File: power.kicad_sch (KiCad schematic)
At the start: 4 parts

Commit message: working on powers
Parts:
- added C17: C-Pol-10uF-TAN, Capacitor_Tantalum_SMD:CP_EIA-6032-28_Kemet-C, symbol eurorack:C-Pol-10uF-TAN
- added RV11: Trim_5k_prec_tht, eurorack:trim_2.5mm, symbol eurorack:Trim_5k_prec_tht
- added U10: TL072, Package_SO:SO-8_3.9x4.9mm_P1.27mm, symbol eurorack:TL072
- added U9: ZLDO1117G33TA, Package_TO_SOT_SMD:SOT-223, symbol eurorack:ZLDO1117G33TA
- gave numbers to parts that had none: 4
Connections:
- net +12V: now also U10.8 (V+)
- net +5V: now also U9.3 (IN)
- net -12V: now also RV11.3, U10.4 (V-)
- net GND: now also C17.2, RV11.1, U10.5 (+), U9.1 (ADJ)
- new net: RV11.2, U10.3 (+)
- new net: U10.6 (-), U10.7
- new net +3V3: C17.1, U9.2 (OUT), U9.4 (OUT)
- new net -1V65: U10.1, U10.2 (-)

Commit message: WIP
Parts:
- added C?: C-Pol-1uF-FK-V, Capacitor_SMD:C_1206_3216Metric, symbol eurorack:C-Pol-1uF-FK-V
- added C?: C-Pol-10uF-FK-V, Capacitor_SMD:CP_Elec_8x6.2, symbol eurorack:C-Pol-10uF-FK-V
- added C? (x2): C-100nF-0805, Capacitor_SMD:C_0805_2012Metric_Pad1.18x1.45mm_HandSolder, symbol eurorack:C-100nF-0805
- added U?: REF191, Package_SO:SO-8_3.9x4.9mm_P1.27mm, symbol eurorack:REF191
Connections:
- net +3V3: now also C?.1, C?.1, U?.2 (Vin), U?.3 (~{Sleep})
- net GND: now also C?.2, C?.2, C?.2, C?.2, U?.4 (GND)
- new net 1V25: C?.1, C?.1, U?.6 (Vout)

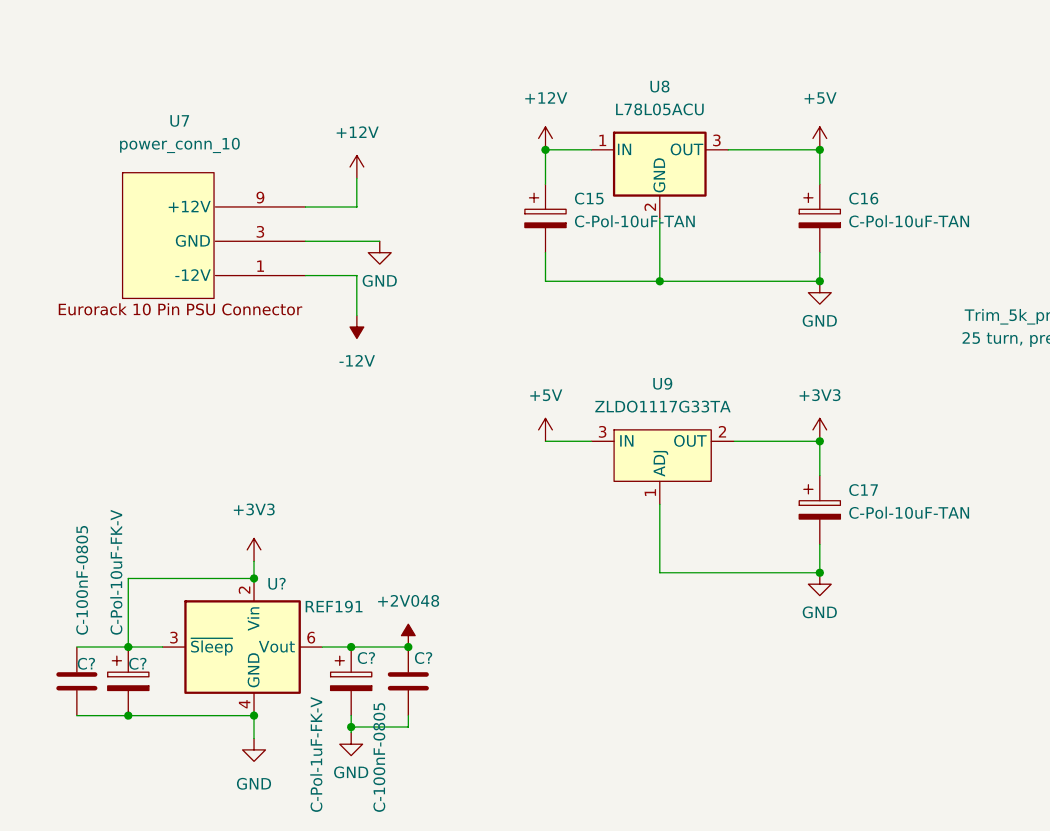
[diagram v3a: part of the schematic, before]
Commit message: refactoring with global labels
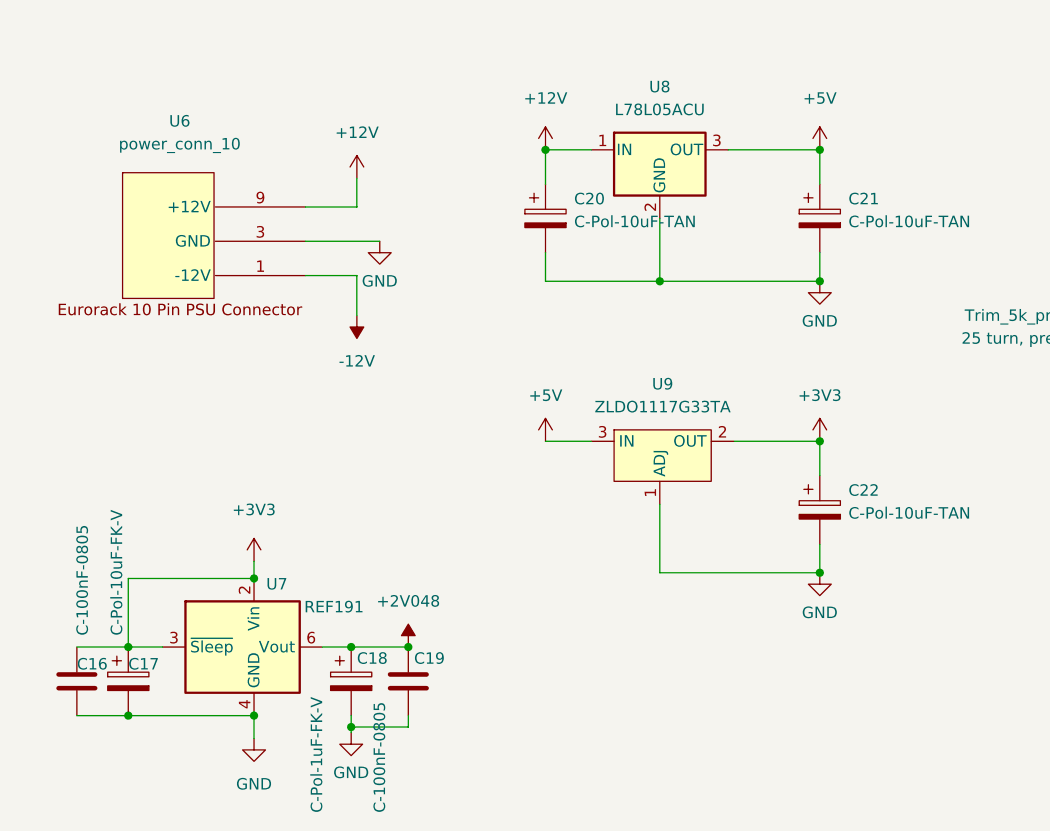
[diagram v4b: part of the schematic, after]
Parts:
- gave numbers to parts that had none: 5
- renumbered C15 to C20, C16 to C21, C17 to C22, U7 to U6
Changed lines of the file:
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@@
   (symbol (lib_id "eurorack:power_conn_10") (at 37.465 32.385 0) (unit 1)
     (in_bom yes) (on_board yes) (fields_autoplaced)
-    (property "Reference" "U7" (id 0) (at 38.735 25.4 0))
+    (property "Reference" "U6" (id 0) (at 38.735 25.4 0))
     (property "Value" "power_conn_10" (id 1) (at 38.735 27.94 0))
     (property "Footprint" "eurorack:power_10" (id 2) (at 40.005 48.895 0)
@@
   (symbol (lib_id "power:-12V") (at 143.51 52.705 180) (unit 1)
     (in_bom yes) (on_board yes) (fields_autoplaced)
-    (property "Reference" "#PWR070" (id 0) (at 143.51 55.245 0)
+    (property "Reference" "#PWR080" (id 0) (at 143.51 55.245 0)
       (effects (font (size 1.27 1.27)) hide)
     )
@@
   (symbol (lib_id "power:+12V") (at 79.375 28.575 0) (unit 1)
     (in_bom yes) (on_board yes) (fields_autoplaced)
-    (property "Reference" "#PWR064" (id 0) (at 79.375 32.385 0)
+    (property "Reference" "#PWR074" (id 0) (at 79.375 32.385 0)
       (effects (font (size 1.27 1.27)) hide)
     )
@@
   (symbol (lib_id "power:GND") (at 109.855 75.565 0) (unit 1)
     (in_bom yes) (on_board yes) (fields_autoplaced)
-    (property "Reference" "#PWR069" (id 0) (at 109.855 81.915 0)
+    (property "Reference" "#PWR079" (id 0) (at 109.855 81.915 0)
       (effects (font (size 1.27 1.27)) hide)
     )
@@
   (symbol (lib_id "power:+5V") (at 79.375 60.96 0) (unit 1)
     (in_bom yes) (on_board yes) (fields_autoplaced)
-    (property "Reference" "#PWR065" (id 0) (at 79.375 64.77 0)
+    (property "Reference" "#PWR075" (id 0) (at 79.375 64.77 0)
       (effects (font (size 1.27 1.27)) hide)
     )
@@
   (symbol (lib_id "eurorack:C-Pol-1uF-FK-V") (at 57.785 87.63 0) (unit 1)
     (in_bom yes) (on_board yes)
-    (property "Reference" "C?" (id 0) (at 58.42 85.09 0)
+    (property "Reference" "C18" (id 0) (at 58.42 85.09 0)
       (effects (font (size 1.27 1.27)) (justify left))
     )
@@
   (symbol (lib_id "power:GND") (at 46.99 93.98 0) (unit 1)
     (in_bom yes) (on_board yes) (fields_autoplaced)
-    (property "Reference" "#PWR?" (id 0) (at 46.99 100.33 0)
+    (property "Reference" "#PWR068" (id 0) (at 46.99 100.33 0)
       (effects (font (size 1.27 1.27)) hide)
     )
@@
   (symbol (lib_id "power:-12V") (at 274.32 38.735 180) (unit 1)
     (in_bom yes) (on_board yes) (fields_autoplaced)
-    (property "Reference" "#PWR075" (id 0) (at 274.32 41.275 0)
+    (property "Reference" "#PWR085" (id 0) (at 274.32 41.275 0)
       (effects (font (size 1.27 1.27)) hide)
     )
@@
   (symbol (lib_id "eurorack:C-Pol-10uF-TAN") (at 109.855 36.195 0) (unit 1)
     (in_bom yes) (on_board yes) (fields_autoplaced)
-    (property "Reference" "C16" (id 0) (at 113.03 34.0359 0)
+    (property "Reference" "C21" (id 0) (at 113.03 34.0359 0)
       (effects (font (size 1.27 1.27)) (justify left))
     )
@@
   (symbol (lib_id "eurorack:C-Pol-10uF-FK-V") (at 33.02 87.63 0) (unit 1)
     (in_bom yes) (on_board yes)
-    (property "Reference" "C?" (id 0) (at 33.02 85.725 0)
+    (property "Reference" "C17" (id 0) (at 33.02 85.725 0)
       (effects (font (size 1.27 1.27)) (justify left))
     )
@@
   (symbol (lib_id "eurorack:C-100nF-0805") (at 64.135 87.63 0) (unit 1)
     (in_bom yes) (on_board yes)
-    (property "Reference" "C?" (id 0) (at 64.77 85.09 0)
+    (property "Reference" "C19" (id 0) (at 64.77 85.09 0)
       (effects (font (size 1.27 1.27)) (justify left))
     )
@@
   (symbol (lib_id "power:GND") (at 57.785 93.345 0) (unit 1)
     (in_bom yes) (on_board yes) (fields_autoplaced)
-    (property "Reference" "#PWR?" (id 0) (at 57.785 99.695 0)
+    (property "Reference" "#PWR069" (id 0) (at 57.785 99.695 0)
       (effects (font (size 1.27 1.27)) hide)
     )
@@
   (symbol (lib_id "eurorack:C-100nF-0805") (at 27.305 87.63 0) (unit 1)
     (in_bom yes) (on_board yes)
-    (property "Reference" "C?" (id 0) (at 27.305 85.725 0)
+    (property "Reference" "C16" (id 0) (at 27.305 85.725 0)
       (effects (font (size 1.27 1.27)) (justify left))
     )
@@
   (symbol (lib_id "power:+5V") (at 109.855 28.575 0) (unit 1)
     (in_bom yes) (on_board yes) (fields_autoplaced)
-    (property "Reference" "#PWR066" (id 0) (at 109.855 32.385 0)
+    (property "Reference" "#PWR076" (id 0) (at 109.855 32.385 0)
       (effects (font (size 1.27 1.27)) hide)
     )
@@
   (symbol (lib_id "power:+3V3") (at 109.855 60.96 0) (unit 1)
     (in_bom yes) (on_board yes) (fields_autoplaced)
-    (property "Reference" "#PWR068" (id 0) (at 109.855 64.77 0)
+    (property "Reference" "#PWR078" (id 0) (at 109.855 64.77 0)
       (effects (font (size 1.27 1.27)) hide)
     )
@@
   (symbol (lib_id "power:GND") (at 60.96 38.735 0) (unit 1)
     (in_bom yes) (on_board yes) (fields_autoplaced)
-    (property "Reference" "#PWR063" (id 0) (at 60.96 45.085 0)
+    (property "Reference" "#PWR072" (id 0) (at 60.96 45.085 0)
       (effects (font (size 1.27 1.27)) hide)
     )
@@
   (symbol (lib_id "eurorack:C-Pol-10uF-TAN") (at 79.375 36.195 0) (unit 1)
     (in_bom yes) (on_board yes) (fields_autoplaced)
-    (property "Reference" "C15" (id 0) (at 82.55 34.0359 0)
+    (property "Reference" "C20" (id 0) (at 82.55 34.0359 0)
       (effects (font (size 1.27 1.27)) (justify left))
     )
@@
   (symbol (lib_id "power:+3V3") (at 46.99 74.295 0) (unit 1)
     (in_bom yes) (on_board yes) (fields_autoplaced)
-    (property "Reference" "#PWR?" (id 0) (at 46.99 78.105 0)
+    (property "Reference" "#PWR067" (id 0) (at 46.99 78.105 0)
       (effects (font (size 1.27 1.27)) hide)
     )
@@
   (symbol (lib_id "eurorack:C-Pol-10uF-TAN") (at 109.855 68.58 0) (unit 1)
     (in_bom yes) (on_board yes) (fields_autoplaced)
-    (property "Reference" "C17" (id 0) (at 113.03 66.4209 0)
+    (property "Reference" "C22" (id 0) (at 113.03 66.4209 0)
       (effects (font (size 1.27 1.27)) (justify left))
     )
@@
   (symbol (lib_id "eurorack:REF191") (at 46.99 83.82 0) (unit 1)
     (in_bom yes) (on_board yes)
-    (property "Reference" "U?" (id 0) (at 49.53 76.835 0))
+    (property "Reference" "U7" (id 0) (at 49.53 76.835 0))
     (property "Value" "REF191" (id 1) (at 55.88 79.375 0))
     (property "Footprint" "Package_SO:SO-8_3.9x4.9mm_P1.27mm" (id 2) (at 46.99 85.09 0)
@@
   (symbol (lib_id "power:GND") (at 109.855 43.18 0) (unit 1)
     (in_bom yes) (on_board yes) (fields_autoplaced)
-    (property "Reference" "#PWR067" (id 0) (at 109.855 49.53 0)
+    (property "Reference" "#PWR077" (id 0) (at 109.855 49.53 0)
       (effects (font (size 1.27 1.27)) hide)
     )
@@
   (symbol (lib_id "power:+12V") (at 274.32 20.955 0) (unit 1)
     (in_bom yes) (on_board yes) (fields_autoplaced)
-    (property "Reference" "#PWR074" (id 0) (at 274.32 24.765 0)
+    (property "Reference" "#PWR084" (id 0) (at 274.32 24.765 0)
       (effects (font (size 1.27 1.27)) hide)
     )
@@
   (symbol (lib_id "power:GND") (at 148.59 39.37 0) (unit 1)
     (in_bom yes) (on_board yes) (fields_autoplaced)
-    (property "Reference" "#PWR071" (id 0) (at 148.59 45.72 0)
+    (property "Reference" "#PWR081" (id 0) (at 148.59 45.72 0)
       (effects (font (size 1.27 1.27)) hide)
     )
@@
   (symbol (lib_id "power:+12V") (at 58.42 31.75 0) (unit 1)
     (in_bom yes) (on_board yes) (fields_autoplaced)
-    (property "Reference" "#PWR061" (id 0) (at 58.42 35.56 0)
+    (property "Reference" "#PWR070" (id 0) (at 58.42 35.56 0)
       (effects (font (size 1.27 1.27)) hide)
     )
@@
   (symbol (lib_id "power:GND") (at 153.67 77.47 0) (mirror y) (unit 1)
     (in_bom yes) (on_board yes) (fields_autoplaced)
-    (property "Reference" "#PWR072" (id 0) (at 153.67 83.82 0)
+    (property "Reference" "#PWR082" (id 0) (at 153.67 83.82 0)
       (effects (font (size 1.27 1.27)) hide)
     )
@@
   (symbol (lib_id "power:-12V") (at 58.42 46.99 180) (unit 1)
     (in_bom yes) (on_board yes) (fields_autoplaced)
-    (property "Reference" "#PWR062" (id 0) (at 58.42 49.53 0)
+    (property "Reference" "#PWR071" (id 0) (at 58.42 49.53 0)
       (effects (font (size 1.27 1.27)) hide)
     )
@@
   (symbol (lib_id "eurorack:-1V65") (at 175.26 49.53 180) (unit 1)
     (in_bom yes) (on_board yes) (fields_autoplaced)
-    (property "Reference" "#PWR073" (id 0) (at 175.26 52.07 0)
+    (property "Reference" "#PWR083" (id 0) (at 175.26 52.07 0)
       (effects (font (size 1.27 1.27)) hide)
     )
@@
   (symbol (lib_id "eurorack:+2V048") (at 64.135 83.82 0) (unit 1)
     (in_bom yes) (on_board yes) (fields_autoplaced)
-    (property "Reference" "#PWR?" (id 0) (at 64.135 81.28 0)
-      (effects (font (size 1.27 1.27)) hide)
-    )
+    (property "Reference" "#PWR073" (id 0) (at 64.135 81.28 0)
+      (effects (font (size 1.27 1.27)) hide)
+    )

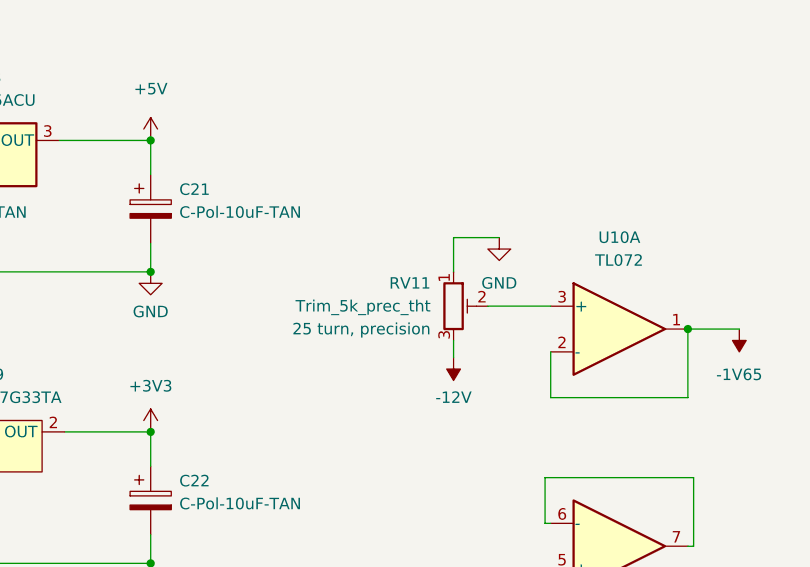
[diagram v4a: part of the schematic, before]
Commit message: cleaning into modules
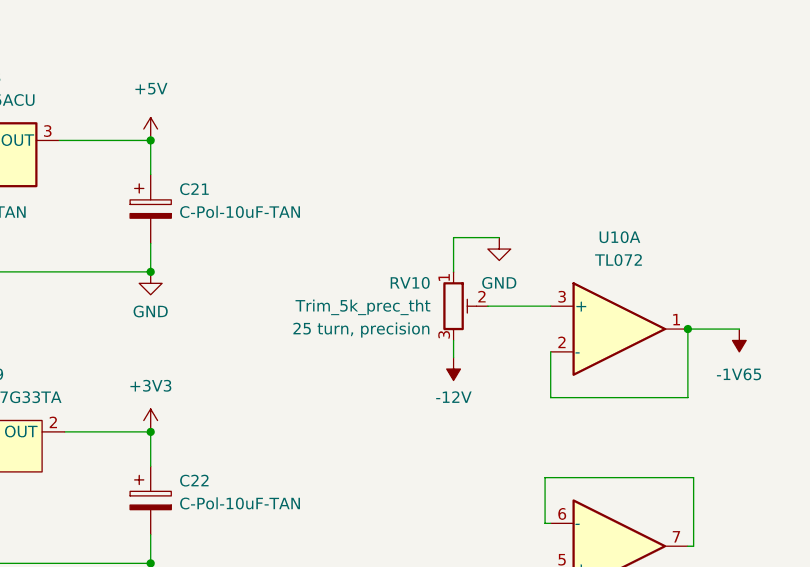
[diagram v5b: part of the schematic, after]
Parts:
- renumbered RV11 to RV10

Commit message: working on AD inputs
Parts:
- removed C18: C-Pol-1uF-FK-V, Capacitor_SMD:C_1206_3216Metric, symbol eurorack:C-Pol-1uF-FK-V
- added C18: C-Pol-1uF-TAN, Capacitor_Tantalum_SMD:CP_EIA-3216-18_Kemet-A, symbol eurorack:C-Pol-1uF-TAN
- renumbered U6 to U20, U7 to U21, U8 to U22, U9 to U23, U10 to U24
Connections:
- net 1V25: now also C18.1
- net GND: now also C18.2
